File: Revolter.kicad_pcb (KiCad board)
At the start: 4 copper layers, 50 x 60 mm, 115 parts, among them IC1 LM5017, IC2 AP65111, IC3 IRSM005, IC4 IRSM005, IC5 IRSM005, J1 Motor, J2 TEMP, J3 USB_B_Mini, P3 IN+, P4 IN-, P5 MOTOR3, P6 MOTOR2, P7 MOTOR1, P8 SWD, Q1 Q_NMOS_GSD, Q2 Q_NMOS_GSD, Q3 Q_NMOS_GSD, U1 STM32F405RGTx, U2 ACS730xLCTR-50AB, U3 ACS730xLCTR-50AB, U4 ACS730xLCTR-50AB, Y1 8MHz

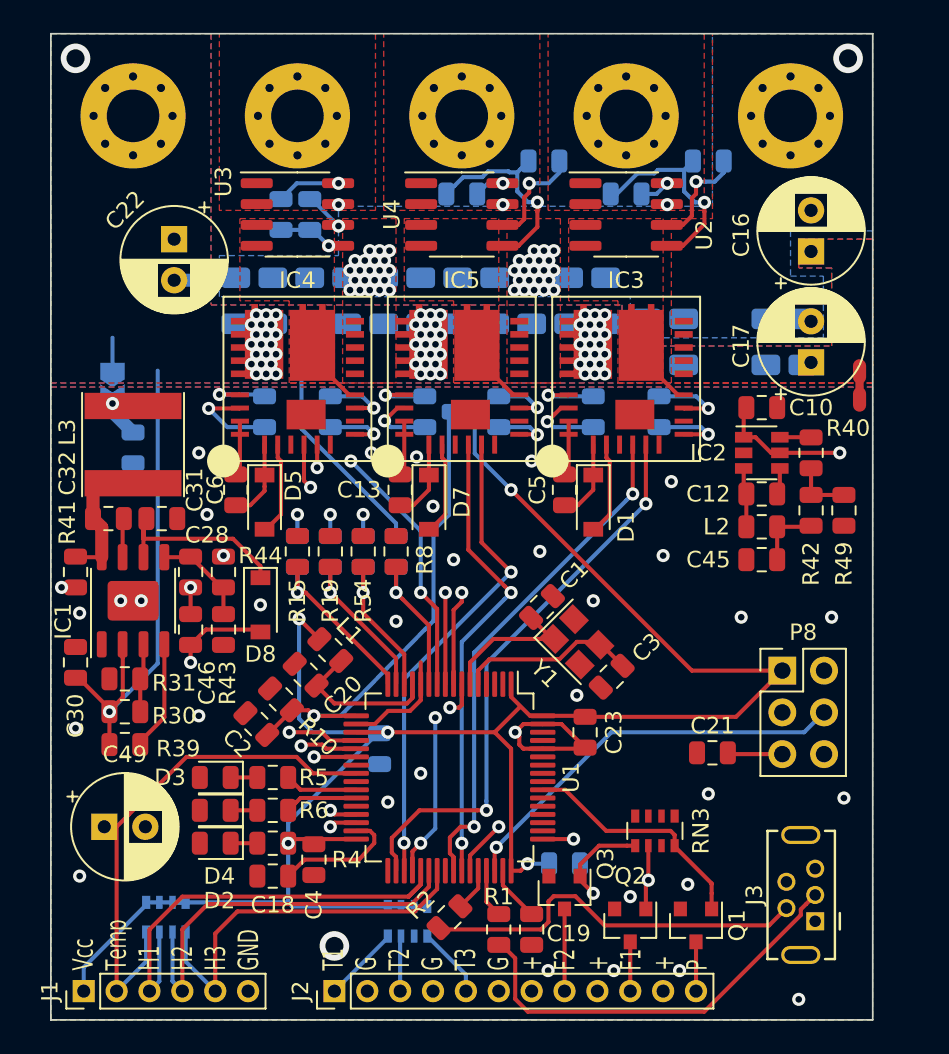
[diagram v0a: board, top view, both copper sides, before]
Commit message: - fixed some polygon bugs - fixed a traces - finishing touches - added version and credits
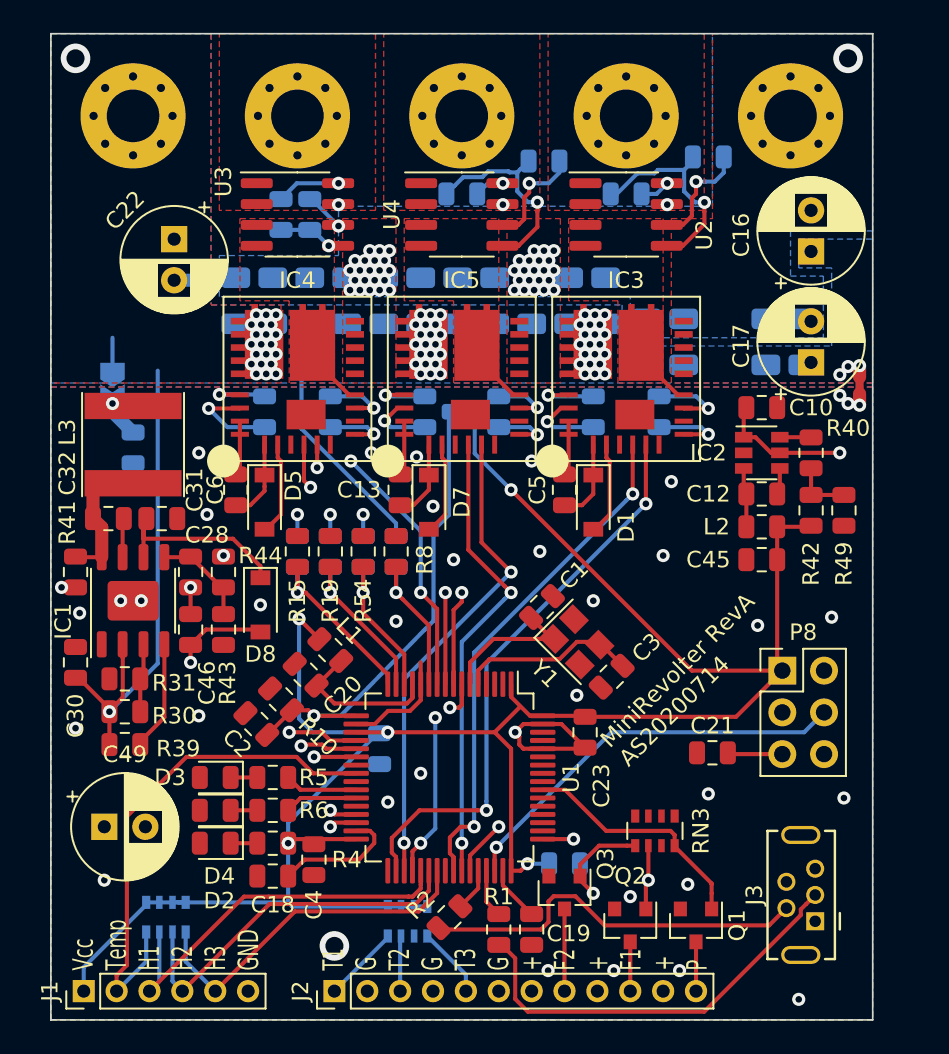
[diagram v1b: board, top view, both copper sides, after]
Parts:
- moved C7 0.25 mm to (175.0, 32.5)
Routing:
- net +3V3: track 214.8 -> 221.6 mm
- net /MCU/HALL_U: track 27.1 -> 24.0 mm
- net /MCU/HALL_V: track 24.7 -> 22.6 mm
- net /MCU/HALL_W: track 23.6 -> 21.7 mm
- net +12V: track 148.1 -> 147.5 mm
- net GND: track 80.3 -> 80.5 mm, vias 38 -> 40
- net GNDPWR: vias 43 -> 46
- added copper zone on Sig, net +BATT
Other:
- board text added: "MiniRevolter RevA AS20200714"

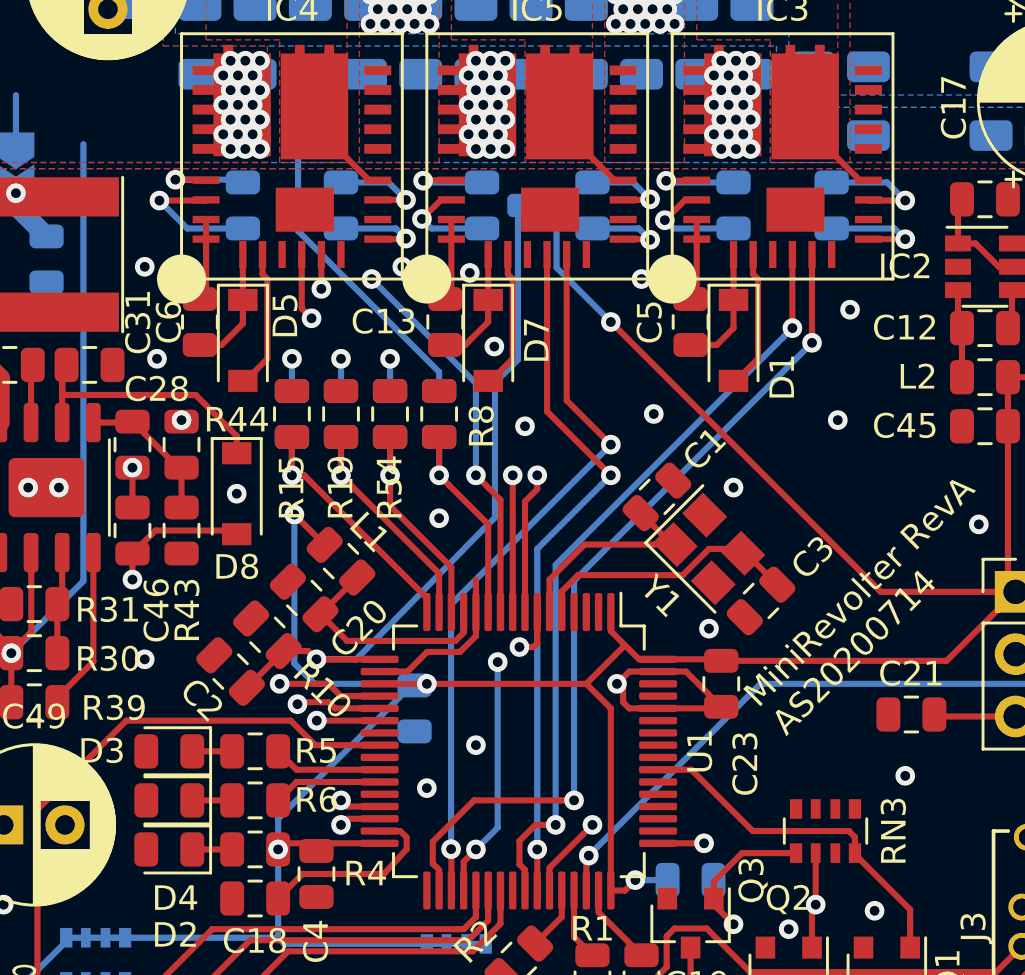
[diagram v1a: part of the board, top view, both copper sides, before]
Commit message: - connected VCC of gatedrivers to VCC (doh)
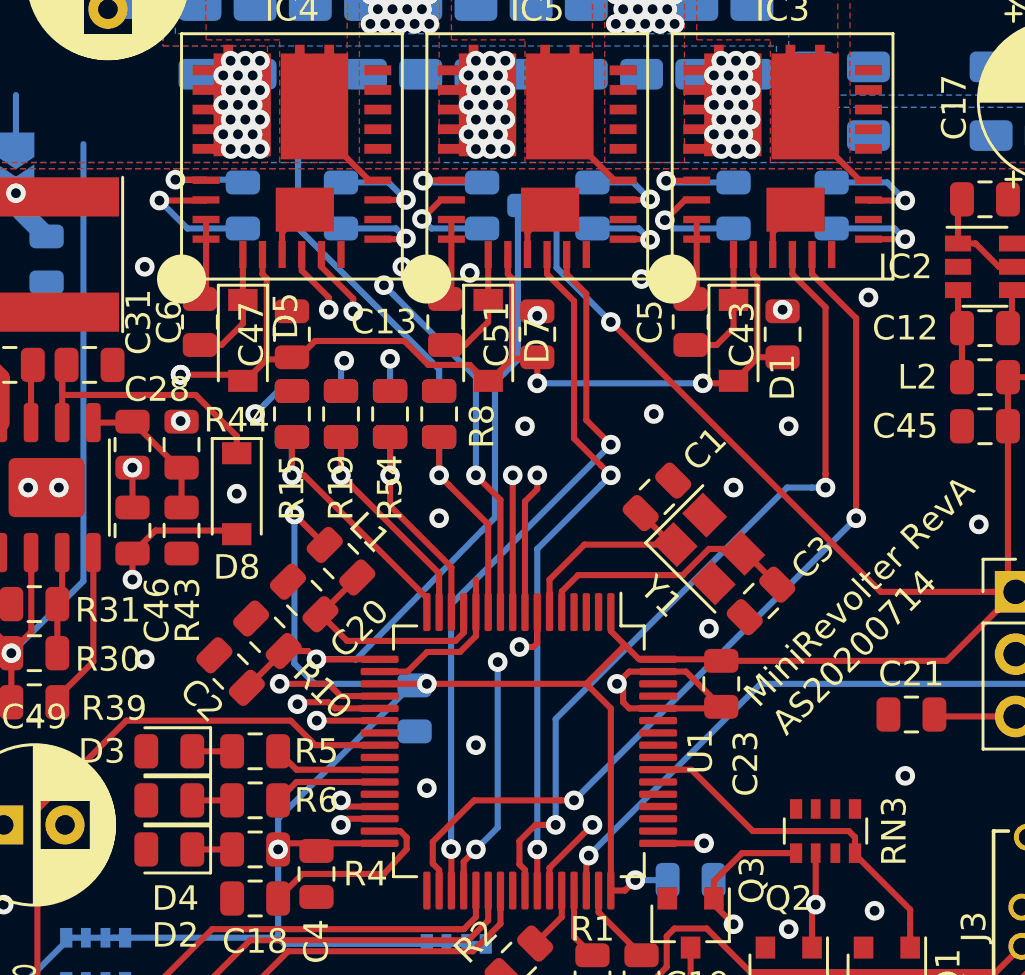
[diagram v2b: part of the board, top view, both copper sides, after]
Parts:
- added C43: 1u, Capacitor_SMD:C_0805_2012Metric, F.Cu at (170.0, 53.2)
- added C47: 1u, Capacitor_SMD:C_0805_2012Metric, F.Cu at (150.0, 53.2)
- added C51: 1u, Capacitor_SMD:C_0805_2012Metric, F.Cu at (160.0, 53.2)
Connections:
- D1 pad 2: Net-(D1-Pad2) -> +12V
- D5 pad 2: Net-(D5-Pad2) -> +12V
- D7 pad 2: Net-(D7-Pad2) -> +12V
- IC3 pad 2: Net-(D1-Pad2) -> +12V
- IC4 pad 2: Net-(D5-Pad2) -> +12V
- IC5 pad 2: Net-(D7-Pad2) -> +12V
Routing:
- net +12V: track 147.5 -> 188.4 mm, vias 4 -> 8
- net GND: track 80.5 -> 87.2 mm
- net Net-(D5-Pad2): track 5.71 -> 0.00 mm
- net Net-(D1-Pad2): track 5.71 -> 0.00 mm
- net Net-(D7-Pad2): track 5.61 -> 0.00 mm
- net /Mosfet driver/Phase_W: track 25.5 -> 29.0 mm
- net /MCU/HU: track 31.1 -> 33.1 mm
- net /MCU/LU: track 34.8 -> 36.3 mm
- net /MCU/LW: track 29.9 -> 30.5 mm
- net /MCU/HW: track 31.6 -> 32.1 mm

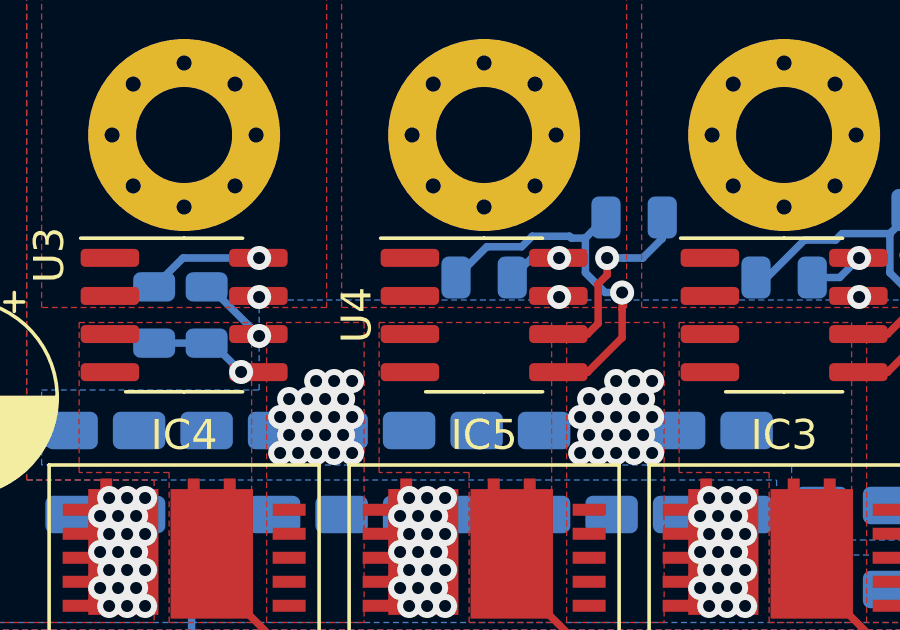
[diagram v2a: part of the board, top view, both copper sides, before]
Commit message: - added jumper under hall for assembly option
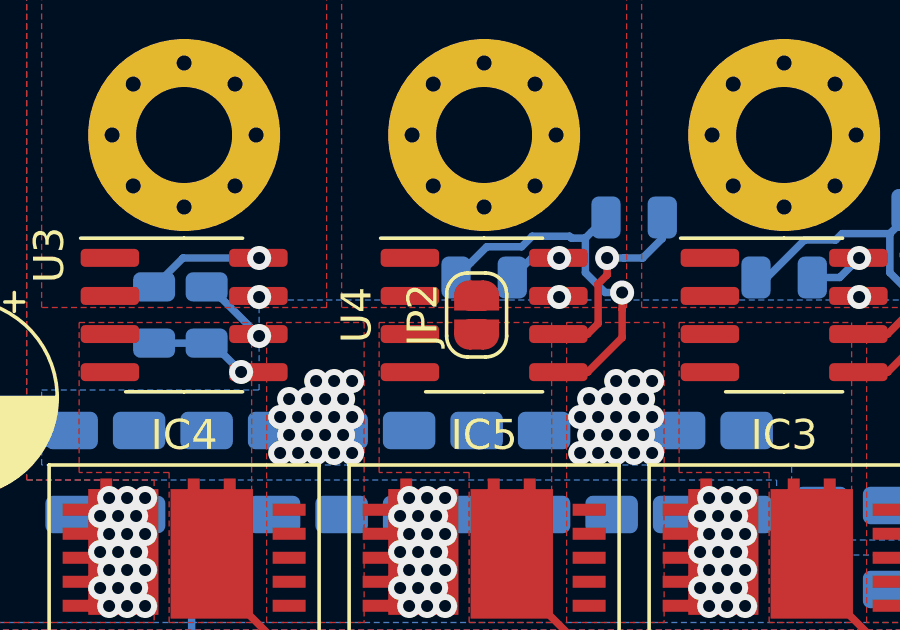
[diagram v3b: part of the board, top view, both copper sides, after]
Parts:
- added JP2: Jumper_NO_Small, Jumper:SolderJumper-2_P1.3mm_Open_RoundedPad1.0x1.5mm, F.Cu at (159.8, 36.0)

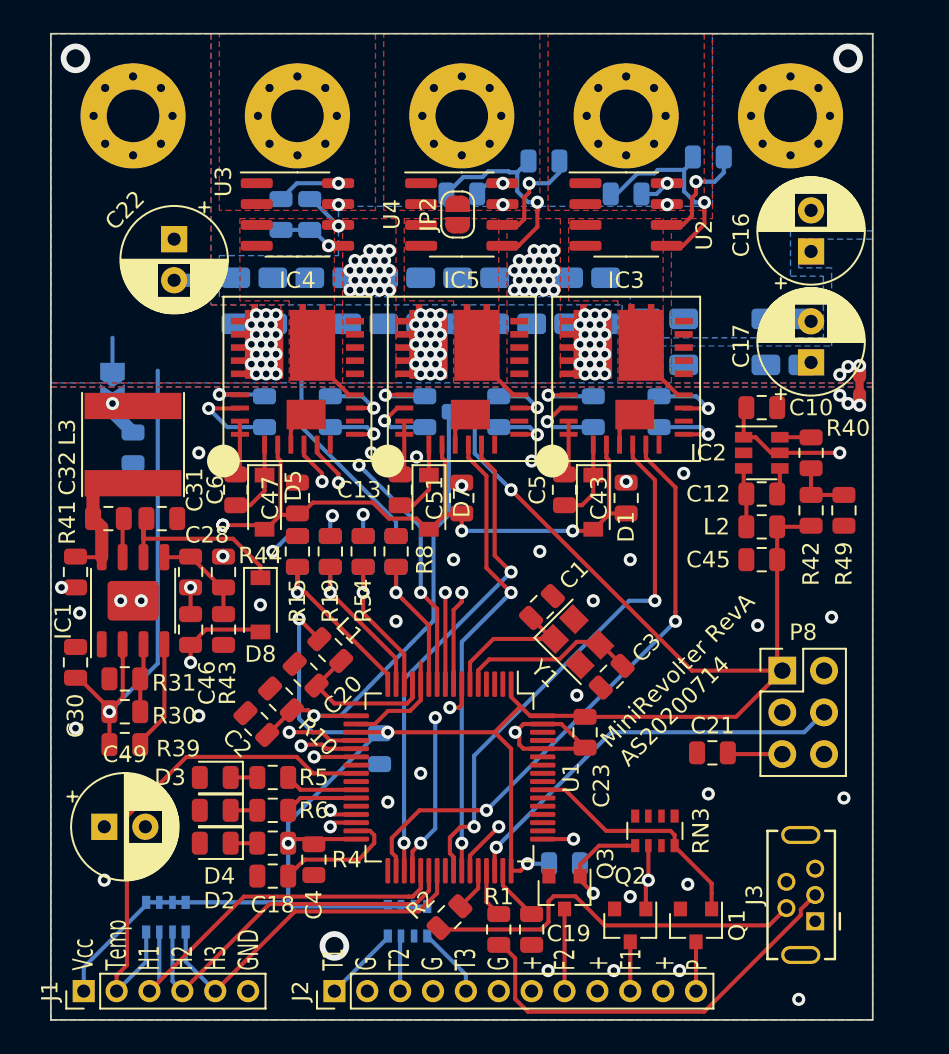
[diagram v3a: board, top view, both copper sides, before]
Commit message: - changed current sensors - updated symbols - exported for production
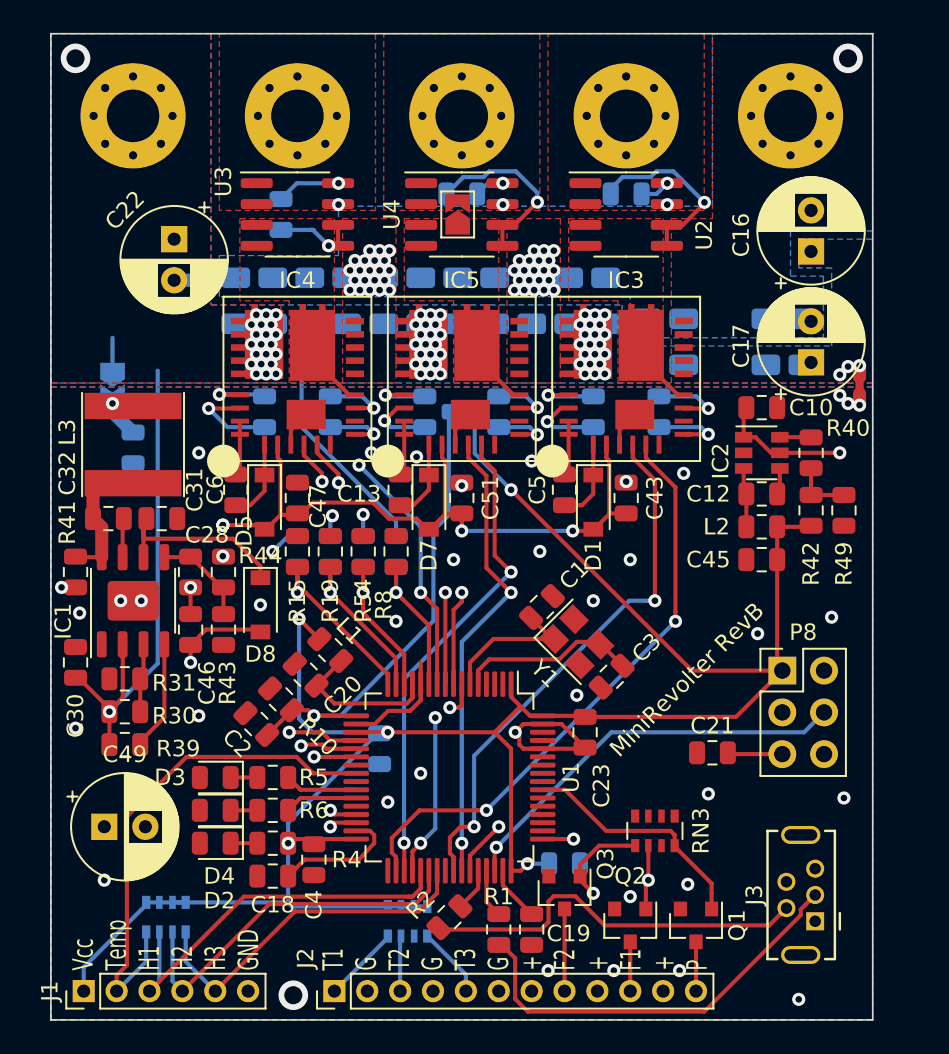
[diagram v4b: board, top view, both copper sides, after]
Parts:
- removed C14, C7, C8: 1n, Capacitor_SMD:C_0805_2012Metric
- JP2: value Jumper_NO_Small -> 2SHUNT; footprint Jumper:SolderJumper-2_P1.3mm_Open_RoundedPad1.0x1.5mm -> Jumper:SolderJumper-2_P1.3mm_Open_TrianglePad1.0x1.5mm
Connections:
- U2 pad 6: Net-(C7-Pad1) -> GND
- U3 pad 6: Net-(C8-Pad1) -> GND
- U4 pad 6: Net-(C14-Pad1) -> GND
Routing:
- net Net-(C7-Pad1): track 6.81 -> 0.00 mm, vias 1 -> 0
- net Net-(C14-Pad1): track 6.59 -> 0.00 mm, vias 1 -> 0
- net Net-(C8-Pad1): track 2.26 -> 0.00 mm, vias 1 -> 0
- net GND: track 87.2 -> 85.1 mm
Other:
- board text added: "MiniRevolter RevB"
- board text removed: "MiniRevolter RevA AS20200714"

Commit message: - shrink PCB to 50x50mm
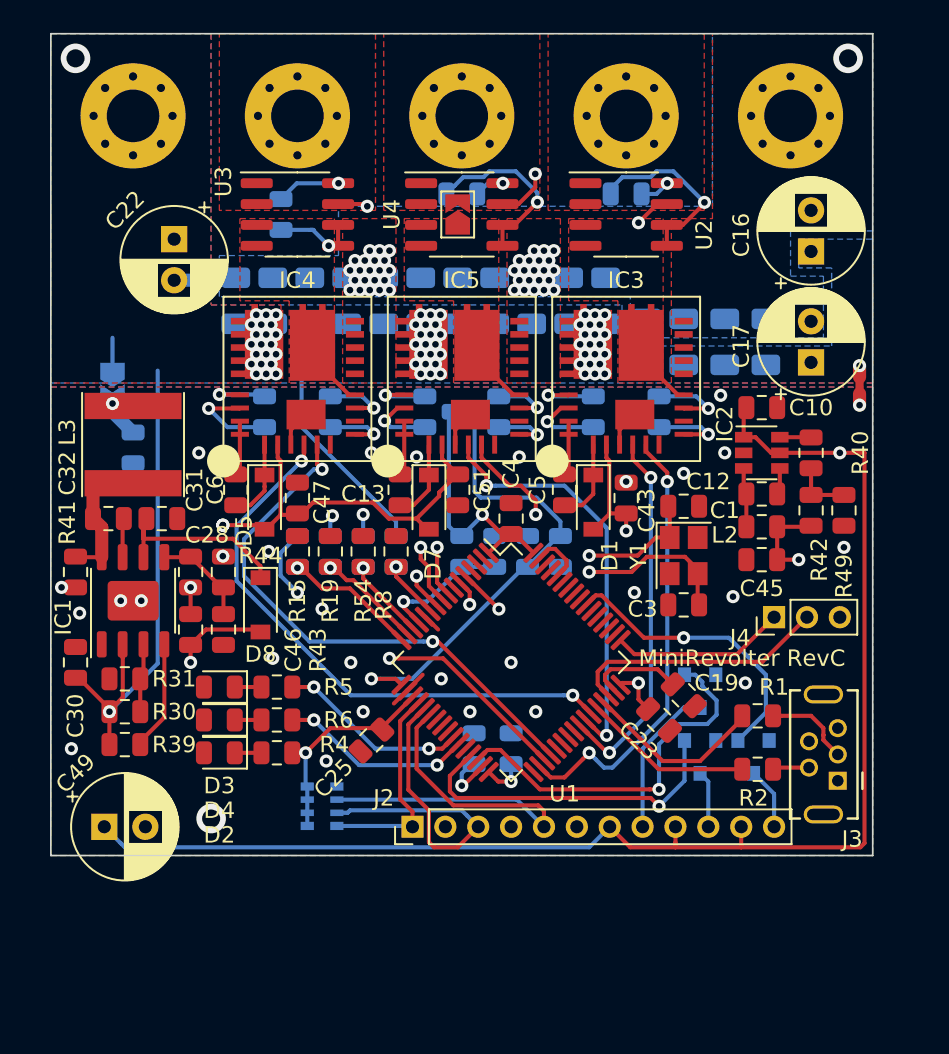
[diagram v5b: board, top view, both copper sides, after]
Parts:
- removed C21: 10n, Capacitor_SMD:C_0805_2012Metric
- removed J1: Motor, Connector_PinHeader_2.00mm:PinHeader_1x06_P2.00mm_Vertical
- removed P8: SWD, Connector_PinHeader_2.54mm:PinHeader_2x03_P2.54mm_Vertical
- removed RN1, RN3: 10k, Resistor_SMD:R_Array_Convex_4x0603
- added J4: Conn_01x03_Male, Connector_PinHeader_2.00mm:PinHeader_1x03_P2.00mm_Vertical, F.Cu at (179.0, 60.5)
- C18, C2, C20, L1, Q1, Q2, Q3, R10: moved to B.Cu
- C25: moved to F.Cu
- moved C4 24.0 mm to (163.0, 54.5), turned to 270 degrees
- moved C2 21.3 mm to (166.0, 56.5), turned to 270 degrees
- moved R2 20.8 mm to (178.0, 69.8), turned to 0 degrees
- moved R1 20.4 mm to (178.0, 66.5), turned to 0 degrees
- moved R10 17.5 mm to (164.0, 56.5), turned to 90 degrees
- moved C19 17.0 mm to (173.5, 65.2), turned to 315 degrees
- moved Q3 14.8 mm to (174.5, 65.0)
- moved C18 14.5 mm to (160.8, 68.5), turned to 270 degrees
- moved C25 13.9 mm to (154.5, 68.0), turned to 45 degrees
- moved C20 13.7 mm to (162.0, 56.5), turned to 270 degrees
- moved Q2 11.1 mm to (174.5, 69.0)
- moved J2 11.1 mm to (157.0, 73.2)
- moved Q1 10.8 mm to (177.8, 69.0)
- moved C1 10.6 mm to (173.5, 53.8), turned to 180 degrees
- moved L1 10.0 mm to (160.0, 56.5), turned to 270 degrees
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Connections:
- RN2 pad 1: /TEMP3 -> (no net)
- RN2 pad 2: (no net) -> /TEMP3
- U1 pad 24: /MCU/TEMP_MOTOR -> (no net)
- U1 pad 37: /MCU/HALL_U -> (no net)
- U1 pad 38: /MCU/HALL_V -> (no net)
- U1 pad 39: /MCU/HALL_W -> (no net)
- U1 pad 7: NRST -> (no net)
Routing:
- net +3V3: track 221.6 -> 109.1 mm, vias 8 -> 9
- net /MCU/TEMP_MOTOR: track 31.1 -> 0.00 mm
- net NRST: track 26.8 -> 0.00 mm, vias 1 -> 0
- net /MCU/HALL_U: track 24.0 -> 0.00 mm
- net /MCU/HALL_V: track 22.6 -> 0.00 mm
- net Net-(J3-Pad2): track 23.9 -> 2.23 mm
- net /MCU/HALL_W: track 21.7 -> 0.00 mm
- net Net-(J3-Pad3): track 25.5 -> 5.34 mm
- net +12V: track 188.4 -> 170.9 mm, vias 8 -> 7
- net /TEMP1: track 27.7 -> 13.0 mm, vias 1 -> 0
- net SWCLK: track 24.0 -> 10.6 mm, vias 1 -> 0
- net /MCU/HU: track 33.1 -> 22.7 mm
- net GND: track 85.1 -> 74.7 mm, vias 40 -> 30
- net /MCU/LU: track 36.3 -> 27.3 mm
- net SWDIO: track 24.8 -> 15.9 mm, vias 1 -> 0
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- added copper zone on Power, net +3V3
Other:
- board size 50 x 60 mm -> 50 x 50 mm
- board text added: "MiniRevolter RevC"
- board text removed: "MiniRevolter RevB"
- board text removed: "Vcc Temp H1 H2 H3 GND"
